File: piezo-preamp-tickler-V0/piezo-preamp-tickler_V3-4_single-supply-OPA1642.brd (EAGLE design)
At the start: 114.3 x 20.1 mm, 60 parts, among them IC1 OPA1642, J1 Battery, Q1 BQ21040, Q2 MMBFJ201, Q5 BQ297X, Q7 DMN2400, SW1 SPDT, SW2-SPST INPUT-select

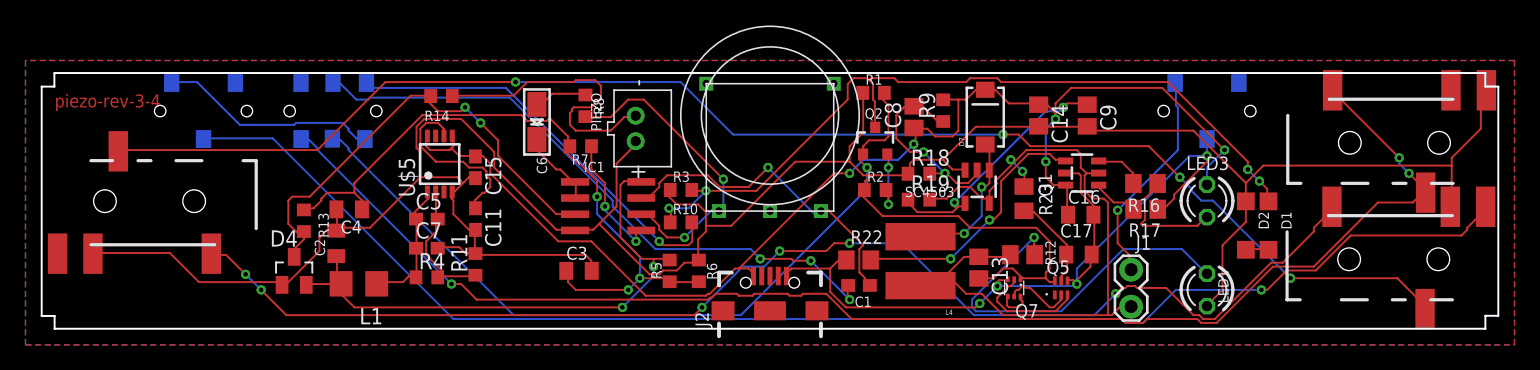
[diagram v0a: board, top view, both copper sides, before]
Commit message: updates to piezo preamp
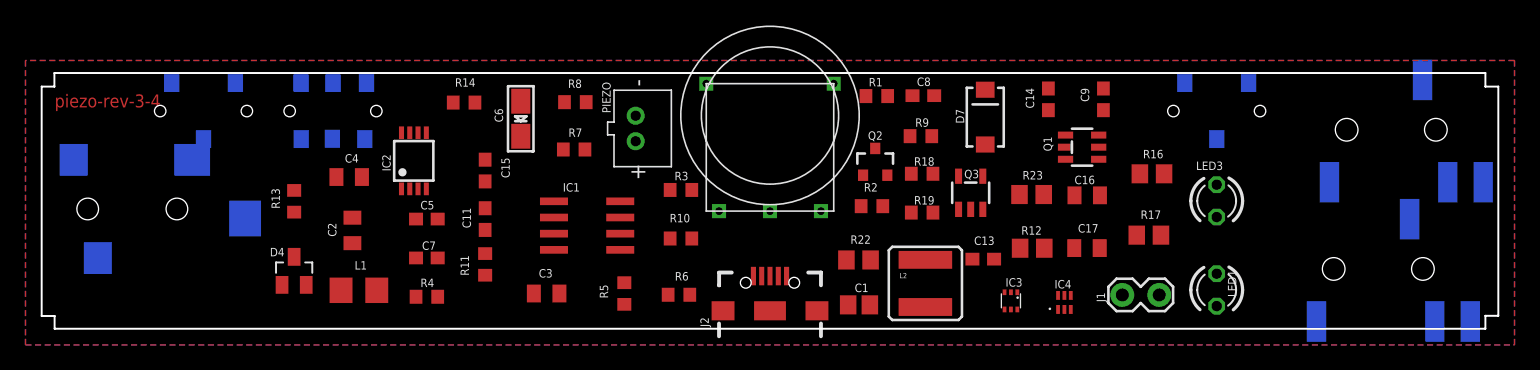
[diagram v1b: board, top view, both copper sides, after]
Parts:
- removed D1, D2: (no value), diode:SOD123
- removed L4: 2.7uH, SparkFun:CR54
- removed Q5: BQ297X, CMU-ArtFab:WSON-6
- removed Q7: DMN2400, CMU-ArtFab:SOT-563
- removed SC4503: VREG12_SOT23-5, CMU-ArtFab:SOT23-5
- removed TO-HEADSET, TO-PHONE, TO-PHONE1: AUDIO-JACK3LGPADS, Daniel:AUDIO-JACK-TRRS-SMD
- removed U$5: TPS7A49, CMU-ArtFab:MSOP-8
- added IC2: TPS7A49, CMU-ArtFab:MSOP-8
- added IC3: DMN2400, CMU-ArtFab:SOT-563
- added IC4: BQ297X, CMU-ArtFab:WSON-6
- added J$1: Phone, CMU-ArtFab:TRRS_SJ-43514-SMT-TR
- added J$2: Headphones, CMU-ArtFab:TRRS_SJ-43514-SMT-TR
- added L2: 2.7uH, SparkFun-Passives:CR54
- added Q3: SC4503, CMU-ArtFab:SOT23-5
- added U$1: Mixer, CMU-ArtFab:TRS_SJ-3524-SMT
- C1: device adafruit:C0603 -> adafruit:C0805
- C13, C14, C8, C9: device adafruit:C0805 -> adafruit:C0603
- moved R5 3.98 mm to (45.7, 2.76)
- moved C3 3.10 mm to (39.6, 2.76)
- moved R9 2.65 mm to (69.0, 15.1), turned to 180 degrees
- moved C4 2.54 mm to (24.1, 11.9)
- moved R6 2.44 mm to (50.0, 2.67), turned to 180 degrees
- moved IC1 2.25 mm to (42.8, 8.10)
- moved R17 2.05 mm to (86.9, 7.34)
- moved Q1 2.03 mm to (81.6, 14.2)
- moved R14 1.85 mm to (33.1, 17.7)
- moved C8 1.83 mm to (69.2, 18.3), turned to 0 degrees
- moved C9 1.80 mm to (83.3, 18.0)
- moved R13 1.70 mm to (19.8, 10.0)
- moved Q2 1.65 mm to (65.4, 13.0)
- moved C2 1.63 mm to (24.4, 7.71)
- moved C16 1.61 mm to (82.0, 10.5)
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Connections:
- removed net N$1: D1.A, D2.A
- net +12V: now also IC2.1; no longer U$5.1
- net GND: now also IC2.4, IC3.1, IC4.6, J$1.TIP, J$2.TIP, Q3.2, U$1.1; no longer D2.C, Q5.6, Q7.1, SC4503.3, TO-HEADSET.RING2, TO-PHONE.RING2, TO-PHONE1.EARTH, U$5.4
- net GND2: now also IC3.3, IC4.4; no longer Q5.4, Q7.3
- net N$10: no longer D1.C
- net N$12: now also U$1.2, U$1.3, U$1.4; no longer TO-PHONE1.RING1, TO-PHONE1.TIP
- net N$13: now also J$1.RING1, J$2.RING1; no longer TO-HEADSET.TIP, TO-PHONE.TIP
- net N$15: now also J$1.RING2, J$2.RING2; no longer TO-HEADSET.RING1, TO-PHONE.RING1
- net N$17: now also J$1.EARTH; no longer TO-PHONE.EARTH
- net N$26: now also IC2.2; no longer U$5.2
- net N$28: now also IC2.6; no longer U$5.6
- net N$29: now also Q3.4; no longer SC4503.4
- net N$30: now also Q3.3; no longer SC4503.2
- net N$32: now also L2.P$2, Q3.1; no longer L4.P$2, SC4503.1
- net N$4: now also J$2.EARTH; no longer TO-HEADSET.EARTH
- net N$42: now also IC4.5; no longer Q5.5
- net N$43: now also IC3.4, IC3.6; no longer Q7.4, Q7.6
- net N$44: now also IC3.5, IC4.2; no longer Q5.2, Q7.5
- net N$45: now also IC3.2, IC4.3; no longer Q5.3, Q7.2
- net V+: now also IC2.5, IC2.8; no longer U$5.5, U$5.8
- net VBAT: now also L2.P$1, Q3.5; no longer L4.P$1, SC4503.5
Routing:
- net GND: track 229.3 -> 0.00 mm
- net N$15: track 112.5 -> 0.00 mm, vias 4 -> 0
- net N$17: track 110.7 -> 0.00 mm, vias 1 -> 0
- net N$12: track 110.7 -> 0.00 mm, vias 3 -> 0
- net N$13: track 100.7 -> 0.00 mm, vias 6 -> 0
- net V+: track 98.9 -> 0.00 mm, vias 5 -> 0
- net N$10: track 63.5 -> 0.00 mm, vias 4 -> 0
- net GND2: track 63.1 -> 0.00 mm, vias 4 -> 0
- net SELECT: track 61.6 -> 0.00 mm, vias 1 -> 0
- net VBAT: track 60.1 -> 0.00 mm, vias 2 -> 0
- net N$23: track 52.5 -> 0.00 mm, vias 3 -> 0
- net N$16: track 49.2 -> 0.00 mm, vias 3 -> 0
- net N$25: track 44.0 -> 0.00 mm, vias 2 -> 0
- net N$9: track 36.7 -> 0.00 mm, vias 2 -> 0
- net N$11: track 32.5 -> 0.00 mm, vias 1 -> 0
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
